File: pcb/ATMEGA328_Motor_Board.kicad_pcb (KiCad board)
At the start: 2 copper layers, 77 x 100 mm, 249 parts, among them P1 CONN_01X04, P10 CONN_01X04, P11 CONN_01X02, P12 CONN_01X03, P13 CONN_01X02, P14 USB_MINI, P15 CONN_01X02, P16 CONN_02X03, P2 CONN_01X04, P3 CONN_01X03, P4 CONN_01X03, P5 CONN_01X03, P6 CONN_01X03, P7 CONN_01X03, P8 CONN_01X03, P9 CONN_01X04, SW1 Pulsador_2p, U1 ATMEGA328, U10 VOM617A, U11 VOM617A, U12 ASSR-1218, U13 ASSR-1218, U2 PCA9685, U3 FT231X, U4 L298P, U5 L298P, U6 TSR_1, U7 LM2903, U8 LM2903, U9 VOM617A, Y1 16MHz

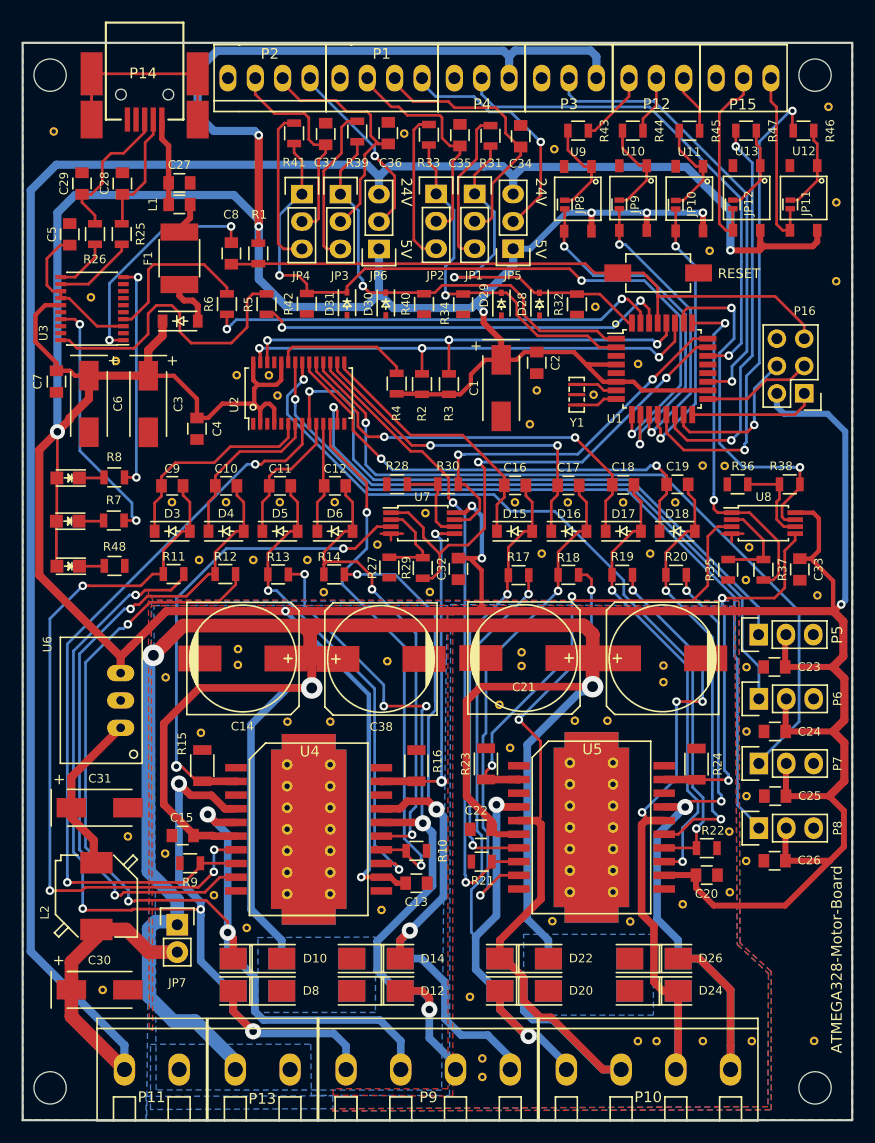
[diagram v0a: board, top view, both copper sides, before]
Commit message: añadidos led para estado y alimentacion externa para salidas digitales
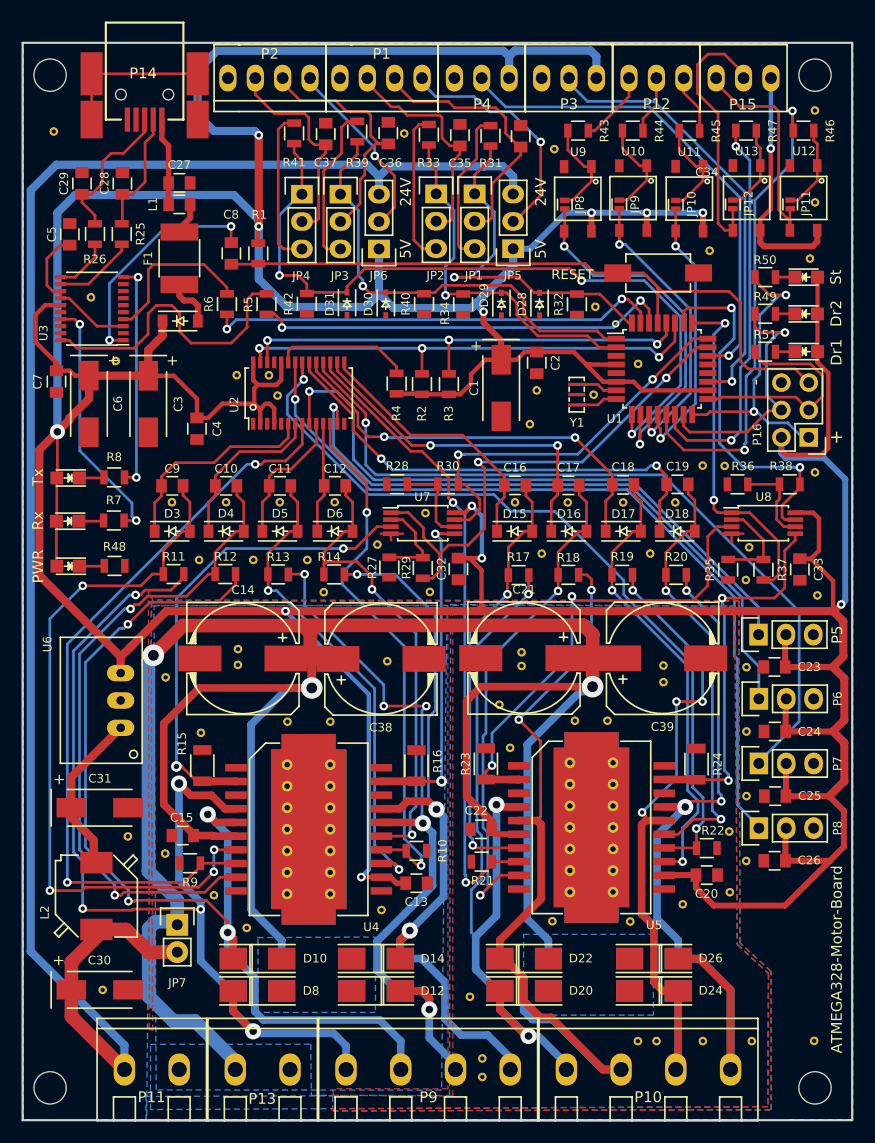
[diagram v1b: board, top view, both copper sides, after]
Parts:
- added D33: Rojo, Leds:LED_0805, F.Cu at (181.2, 65.2)
- added D34: Rojo, Leds:LED_0805, F.Cu at (181.2, 61.8)
- added D35: Rojo, Leds:LED_0805, F.Cu at (181.2, 68.7)
- added Gnd-Via: VAL**, Vias:Gnd-Via, F.Cu at (182.0, 79.9)
- added R49: 270, Resistors_SMD:R_0805, F.Cu at (177.4, 65.2)
- added R50: 270, Resistors_SMD:R_0805, F.Cu at (177.4, 61.8)
- added R51: 270, Resistors_SMD:R_0805, F.Cu at (177.4, 68.7)
- C14, C21, C38, C39: footprint Capacitors_SMD:c_elec_10x10 -> Condensadores:c_elec_10x10
- P15: value CONN_01X02 -> CONN_01X03
- moved G*** 11.5 mm to (118.9, 57.1)
- moved P16 4.10 mm to (181.4, 76.6)
- moved Gnd-Via 3.22 mm to (181.5, 60.0)
- moved Gnd-Via 1.98 mm to (182.0, 54.8)
- moved G*** 1.38 mm to (178.5, 120.5)
- moved Gnd-Via 1.31 mm to (182.0, 46.3)
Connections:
- P15 pad 1: DO1 -> DO_COM
- P15 pad 3: (no net) -> DO1
- U12 pad 4: +24V -> DO_COM
- U13 pad 4: +24V -> DO_COM
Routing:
- net +24V: track 197.5 -> 159.9 mm, vias 1 -> 0
- net DO_COM: track 0.00 -> 22.4 mm, vias 0 -> 1
- net +5V: track 538.0 -> 555.8 mm
- net MISO: track 11.9 -> 28.0 mm, vias 0 -> 2
- net SCK: track 10.2 -> 21.0 mm
- net MOSI: track 14.5 -> 24.2 mm
- net DO2: track 18.3 -> 25.0 mm
- net RESET: track 59.8 -> 65.1 mm
- net DO1: track 17.3 -> 20.8 mm
- net Net-(D35-Pad1): track 0.00 -> 1.82 mm
- net Net-(D34-Pad1): track 0.00 -> 1.81 mm
- net Net-(D33-Pad1): track 0.00 -> 1.81 mm
- net CONSIGNA1: track 42.1 -> 41.3 mm
- net CONSIGNA2: track 46.6 -> 45.9 mm
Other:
- rule pad_to_mask_clearance: 0.2 -> 0.0762
- board text added: "+"
- board text added: "-"
- board text added: "COM"
- board text added: "Dr1"
- board text added: "Dr2"
- board text added: "ENCODER 1 CFG"
- board text added: "ENCODER 2 CFG"
- board text added: "PD2 (D2) : ENCODER 1 CH A PD3 (D3) : ENCODER 2 CH A PD4 (D4) : ENCODER 1 CH B PD5 (D5) : ENCODER 2 CH B PD6 (D6) : DIGITAL IN 1 PD7 (D7) : DIGITAL IN 2 PB0 (D8) : DIGITAL IN 3 PB1 (D9) : DIGITAL OUT 1 PB2 (D10) : DIGITAL OUT 2 ADC0 (A0) : CONSUMO MOTOR 1 ADC1 (A1) : CONSUMO MOTOR 2 ADC2 (A2) : CONSUMO MOTOR 3 ADC3 (A3) : CONSUMO MOTOR 4 ADC6 (A6) : CONSIGNA 1 ADC7 (A7) : CONSIGNA 2"
- board text added: "Rx"
- board text added: "SERVO1"
- board text added: "SERVO2"
- board text added: "SERVO3"
- board text added: "SERVO4"
- board text added: "St"
- board text added: "Tx"
- board text added: "https://github.com/AntonioMR/ATMEGA328-Motor-Board"

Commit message: revision y generacion de GERBER
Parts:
- JP1, JP2, JP3, JP4, JP5, JP6, P5, P6, P7, P8: footprint Pin_Headers:Pin_Header_Straight_1x03 -> Conectores:Pin_Header_Straight_1x03
- JP7: footprint Pin_Headers:Pin_Header_Straight_1x02 -> Conectores:Pin_Header_Straight_1x02
- P16: footprint Pin_Headers:Pin_Header_Straight_2x03 -> Conectores:Pin_Header_Straight_2x03
- moved Gnd-Via 0.72 mm to (117.8, 69.5)
